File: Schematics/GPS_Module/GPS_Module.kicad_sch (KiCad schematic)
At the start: 0 parts

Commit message: added proccessor and added sam-m10q symbol
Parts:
- added C1: 10uf, Capacitor_THT:C_Radial_D5.0mm_H11.0mm_P2.00mm, symbol Device:C
- added C10, C9: 1uf, Capacitor_SMD:C_0402_1005Metric, symbol Device:C
- added C2, C4, C6, C7: 100nf, Capacitor_SMD:C_0402_1005Metric, symbol Device:C
- added C3, C5: 10pF, Capacitor_SMD:C_0402_1005Metric, symbol Device:C
- added C8: 10nf, Capacitor_SMD:C_0402_1005Metric, symbol Device:C
- added FB1: 120R, Inductor_SMD:L_0603_1608Metric, symbol Device:FerriteBead
- added U1: STM32F103CBTx, Package_QFP:LQFP-48_7x7mm_P0.5mm, symbol MCU_ST_STM32F1:STM32F103CBTx
- added U2: SAM-M10Q-00B, SAM-M10Q_UBL, symbol sam-m10q:SAM-M10Q-00B
- added Y1: 16MHz, Crystal:Crystal_SMD_2016-4Pin_2.0x1.6mm, symbol Device:Crystal_GND24
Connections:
- new net +3.3V: C1.1, C1.2, C10.1, C10.2, C2.1, C2.2, C3.2, C4.1, C4.2, C5.2, C6.1, C6.2, C7.1, C7.2, C8.2, C9.2, FB1.2, U1.1 (VBAT), U1.23 (VSS), U1.24 (VDD), U1.35 (VSS), U1.36 (VDD), U1.47 (VSS), U1.48 (VDD), U1.8 (VSSA), Y1.2, Y1.4
- new net +3.3VA: C8.1, C9.1, FB1.1, U1.9 (VDDA)
- new net OSC_IN: C3.1, U1.5 (PD0), Y1.1
- new net OSC_OUT: C5.1, U1.6 (PD1), Y1.3
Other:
- note added: "Additional Filtering to the Analogue VDD"
- note added: "CL = (CLcrystal - Cstray)* 2 YXC XL7EL89CKI-111YLC-16M Crystal"
- note added: "Crystal Oscillator"
- note added: "Decoupling Capacitors for VBAT and VDD"
- note added: "One 100nf "high quality ceramic" capacitor for each VDD and VBAT One 10uf electrolytic capacitor for bulk filtering. Place them as close as possible to the IC."

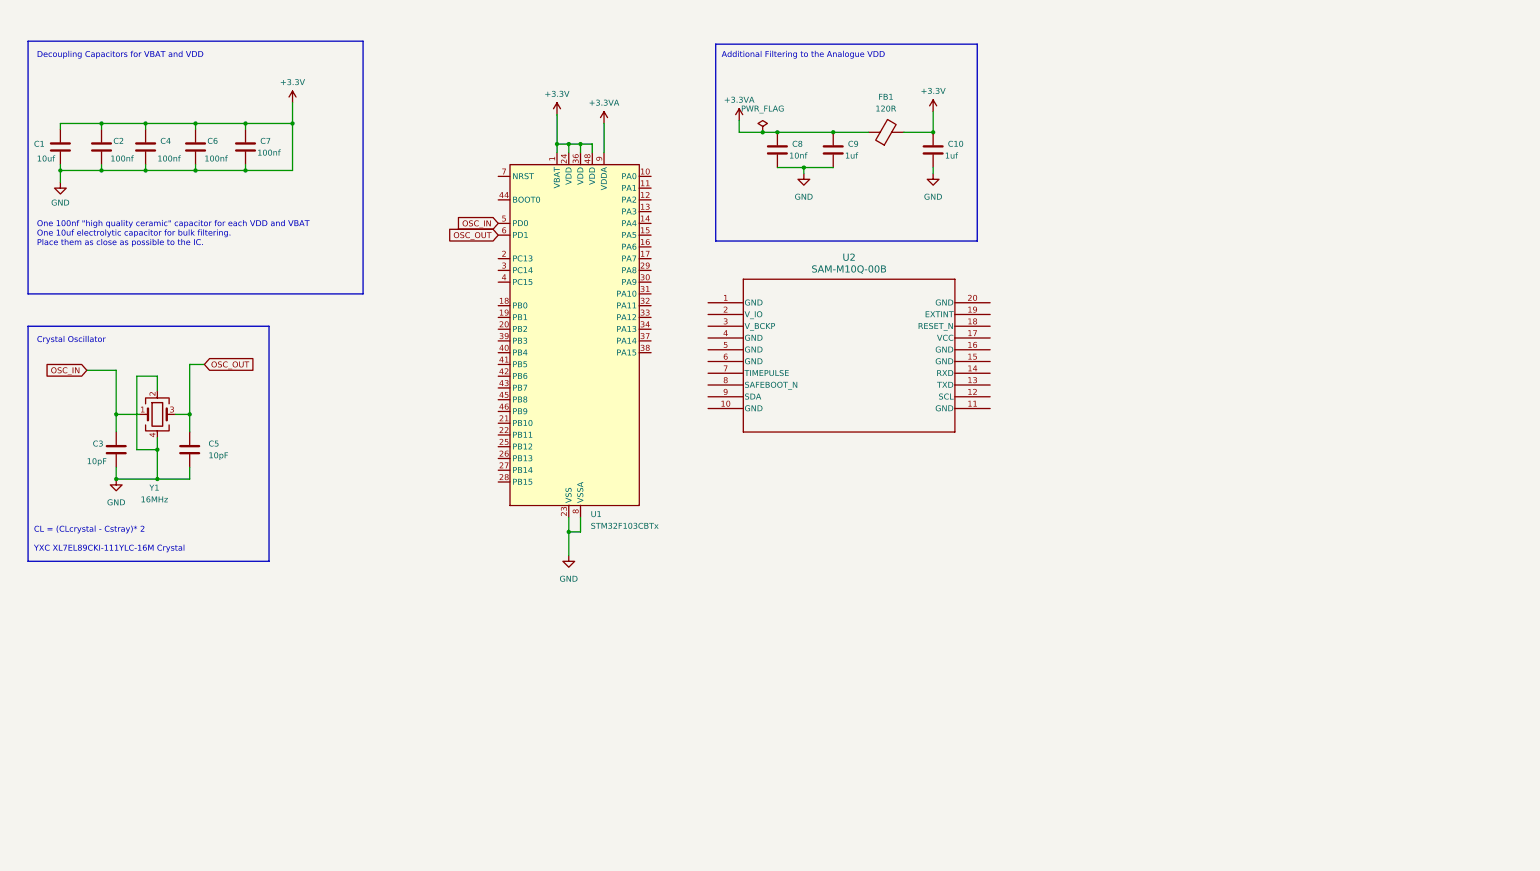
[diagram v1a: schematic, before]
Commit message: added GPS module from last year added labels to processor
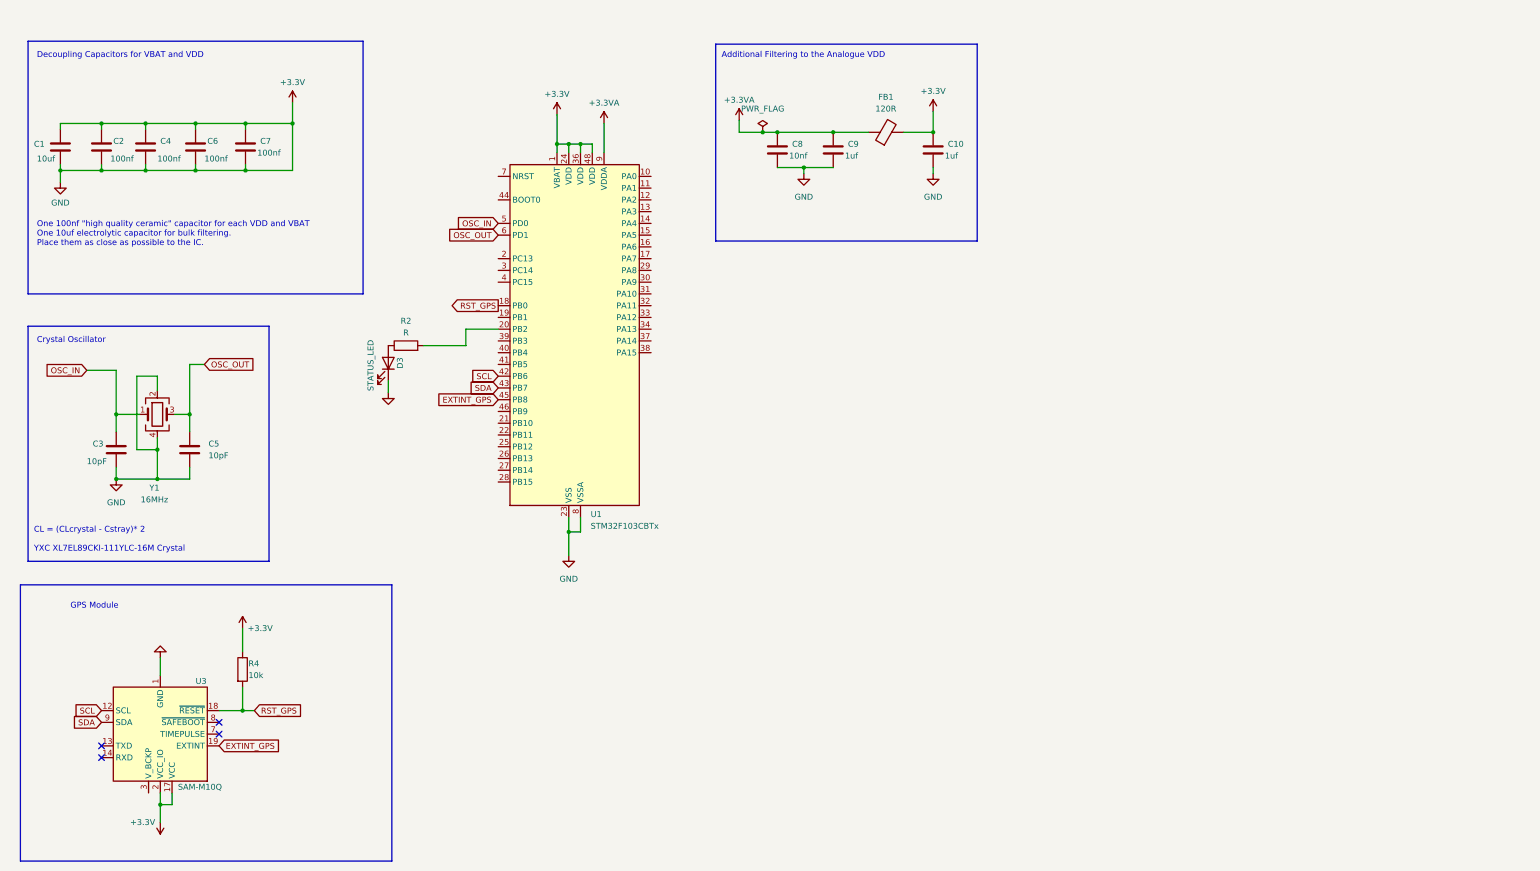
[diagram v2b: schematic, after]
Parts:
- removed U2: SAM-M10Q-00B, SAM-M10Q_UBL, symbol sam-m10q:SAM-M10Q-00B
- added D3: STATUS_LED, LED_SMD:LED_0805_2012Metric, symbol Device:LED
- added R2: R, symbol Device:R
- added R4: 10k, Resistor_SMD:R_0603_1608Metric, symbol Device:R
- added U3: SAM-M10Q, QRET_GPS_Footprints:U-blox_SAM-M8Q, symbol RF_GPS:SAM-M8Q
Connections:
- net +3.3V: now also D3.1 (K), R4.1, U3.1 (GND), U3.10 (GND), U3.11 (GND), U3.15 (GND), U3.16 (GND), U3.17 (VCC), U3.2 (VCC_IO), U3.20 (GND), U3.4 (GND), U3.5 (GND), U3.6 (GND)
- net RST_GPS: now reaches U1.18 (PB0)
- net RST_GPS: now also R4.2, U3.18 (~{RESET})
- net at U1.20 (PB2): now also R2.2
- net SCL: now reaches U1.42 (PB6)
- net SCL: now also U3.12 (SCL)
- net SDA: now reaches U1.43 (PB7)
- net SDA: now also U3.9 (SDA)
- net EXTINT_GPS: now reaches U1.45 (PB8)
- net EXTINT_GPS: now also U3.19 (EXTINT)
- new net: D3.2 (A), R2.1
- no-connect marks 0 -> 4
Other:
- note added: "GPS Module"

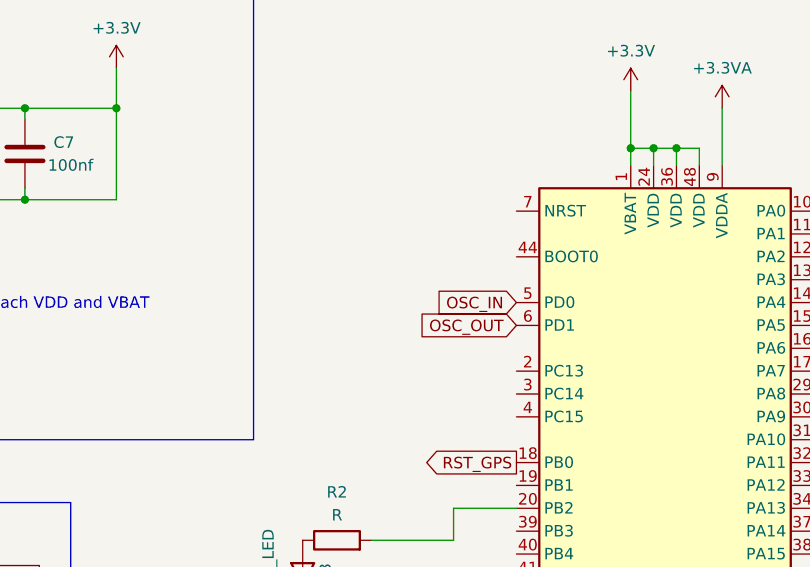
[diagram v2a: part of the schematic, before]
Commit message: Update GPS_Module.kicad_sch
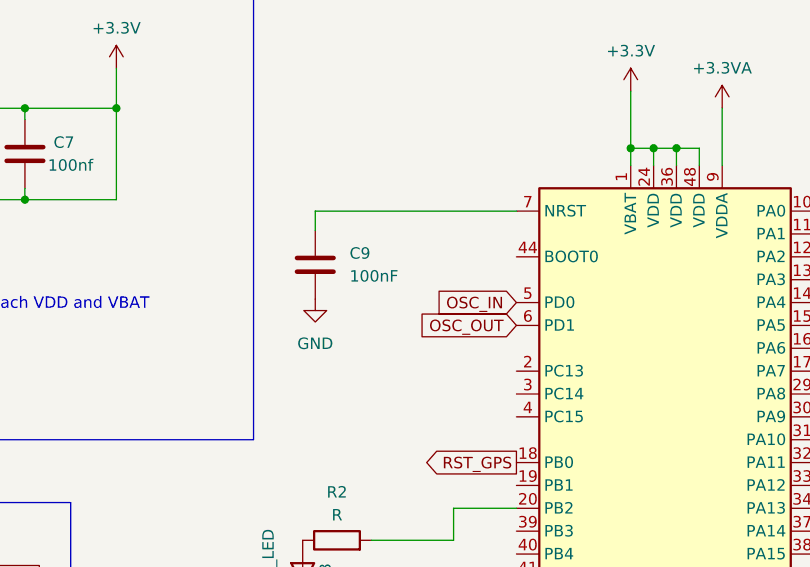
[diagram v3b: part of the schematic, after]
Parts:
- added C9: 100nF, Capacitor_SMD:C_0805_2012Metric, symbol Device:C
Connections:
- net +3.3V: now also C9.2
- net at U1.7 (NRST): now also C9.1
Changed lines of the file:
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@@
+    (stroke (width 0) (type default))
+  )
+  (wire (pts (xy 96.393 47.498) (xy 96.393 49.657))
     (stroke (width 0) (type default))
   )
@@
   )
   (wire (pts (xy 136.525 40.513) (xy 136.525 42.418))
+    (stroke (width 0) (type default))
+  )
+  (wire (pts (xy 118.745 47.498) (xy 96.393 47.498))
     (stroke (width 0) (type default))
   )
@@
         (path "/c9a01778-8bed-4fe7-bd5a-975b80c0ed6a"
           (reference "#PWR012") (unit 1)
+        )
+      )
+    )
+  )
+  (symbol (lib_id "Device:C") (at 96.393 53.467 0) (unit 1)
+    (in_bom yes) (on_board yes) (dnp no)
+    (property "Reference" "C9" (at 100.203 52.197 0)
+      (effects (font (size 1.27 1.27)) (justify left))
+    )
+    (property "Value" "100nF" (at 100.203 54.737 0)
+      (effects (font (size 1.27 1.27)) (justify left))
+    )
+    (property "Footprint" "Capacitor_SMD:C_0805_2012Metric" (at 97.3582 57.277 0)
+      (effects (font (size 1.27 1.27)) hide)
+    )
+    (property "Datasheet" "~" (at 96.393 53.467 0)
+      (effects (font (size 1.27 1.27)) hide)
+    )
+    (property "LCSC" "C49678" (at 96.393 53.467 0)
+      (effects (font (size 1.27 1.27)) hide)
+    )
+    (pin "1")
+    (pin "2")
+    (instances
+      (project "GPS_BOARD_COMPLETE_V1"
+        (path "/9b502ebe-f445-4c9b-a61b-230a013430f4"
+          (reference "C9") (unit 1)
+        )
+      )
+      (project "GPS_Module"
+        (path "/c9a01778-8bed-4fe7-bd5a-975b80c0ed6a"
+          (reference "C11") (unit 1)
         )
       )
@@
         )
       )
+    )
+  )
+  (symbol (lib_id "power:GND") (at 96.393 57.277 0) (unit 1)
+    (in_bom yes) (on_board yes) (dnp no) (fields_autoplaced)
+    (property "Reference" "#PWR015" (at 96.393 63.627 0)
+      (effects (font (size 1.27 1.27)) hide)
+    )
+    (property "Value" "GND" (at 96.393 62.23 0)
+      (effects (font (size 1.27 1.27)))
+    )
+    (property "Footprint" "" (at 96.393 57.277 0)
+      (effects (font (size 1.27 1.27)) hide)
+    )
+    (property "Datasheet" "" (at 96.393 57.277 0)
+      (effects (font (size 1.27 1.27)) hide)
+    )
+    (pin "1")
+    (instances
+      (project "GPS_Module"
+        (path "/c9a01778-8bed-4fe7-bd5a-975b80c0ed6a"
+          (reference "#PWR015") (unit 1)
+        )
+      )

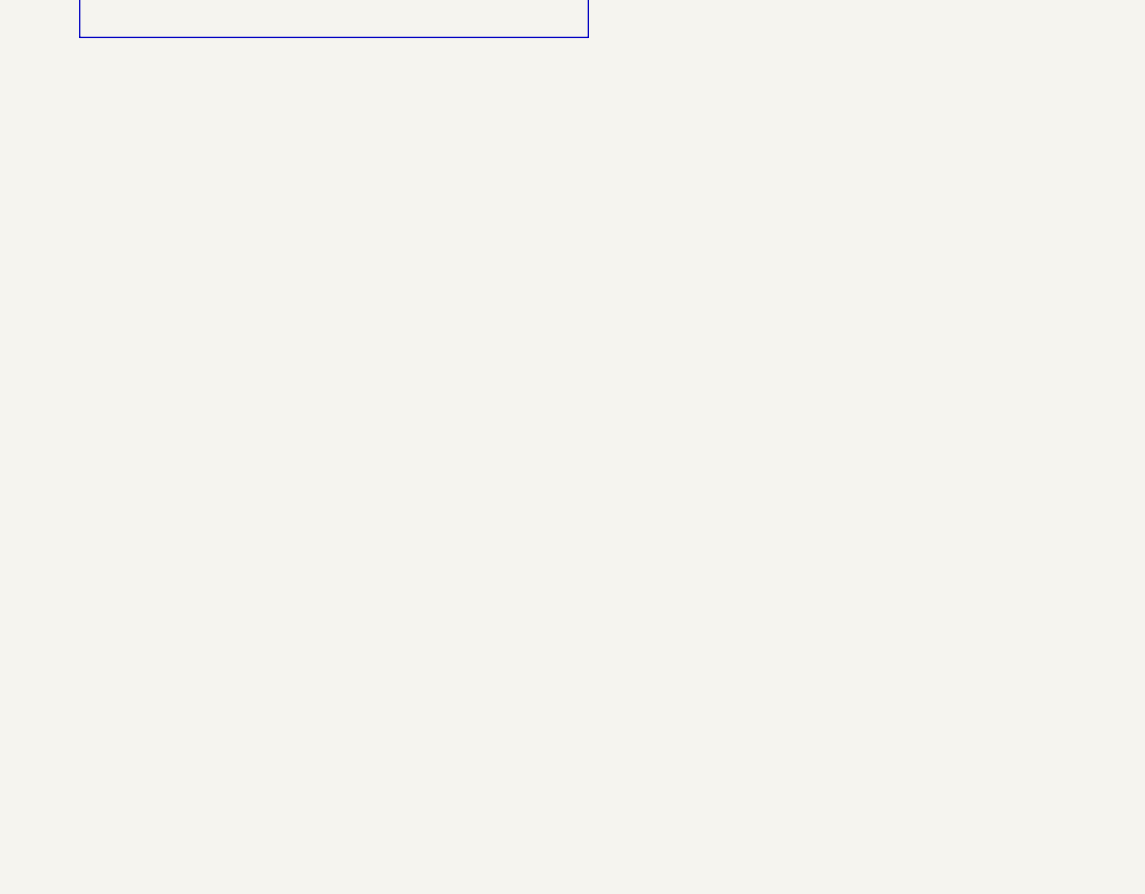
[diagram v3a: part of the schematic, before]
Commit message: Update GPS_Module.kicad_sch
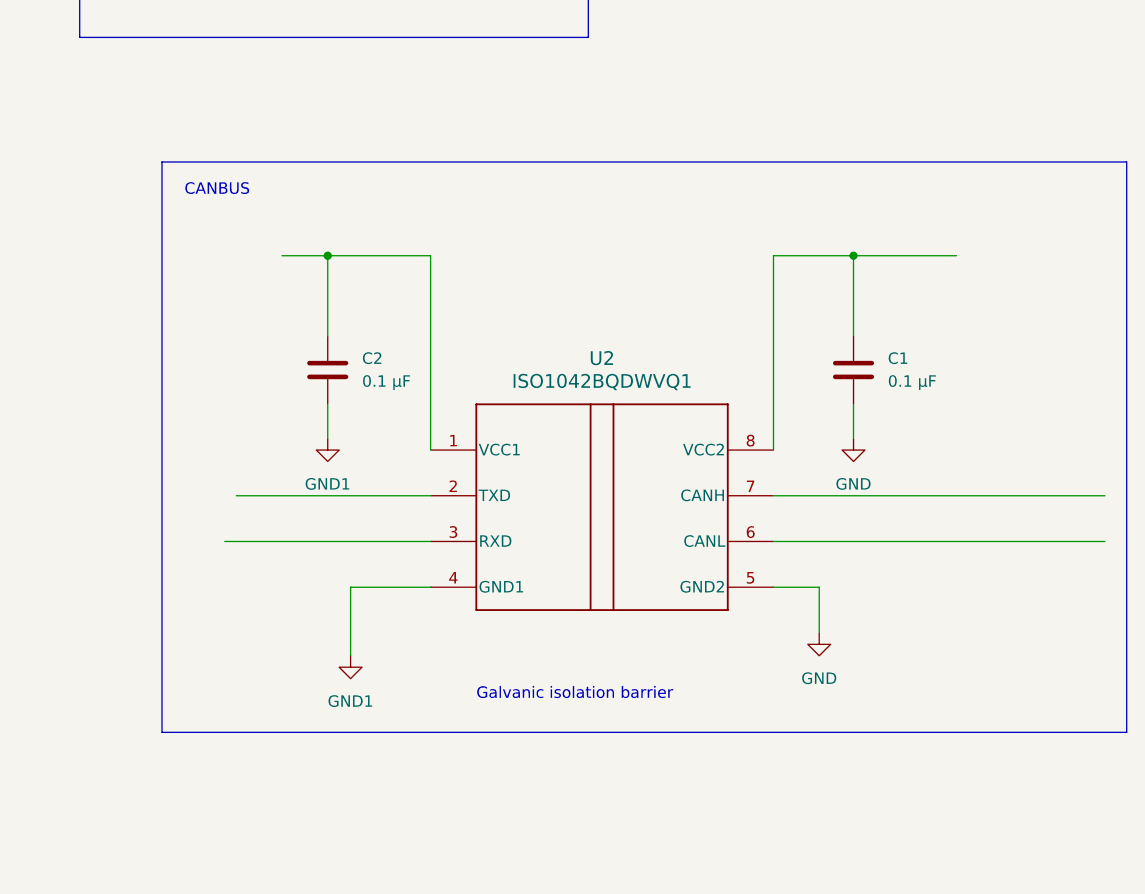
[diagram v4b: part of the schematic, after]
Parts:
- added C1, C2: 0.1 µF, symbol Device:C
- added U2: ISO1042BQDWVQ1, DWV0008A-IPC_A, symbol 2023-11-16_23-22-44:ISO1042BQDWVQ1
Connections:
- net +3.3V: now also C1.2, U2.5 (GND2)
- new net: C1.1, U2.8 (VCC2)
- new net: C2.1, U2.1 (VCC1)
- new net GND1: C2.2, U2.4 (GND1)
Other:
- note added: "CANBUS"
- note added: "Galvanic isolation barrier"

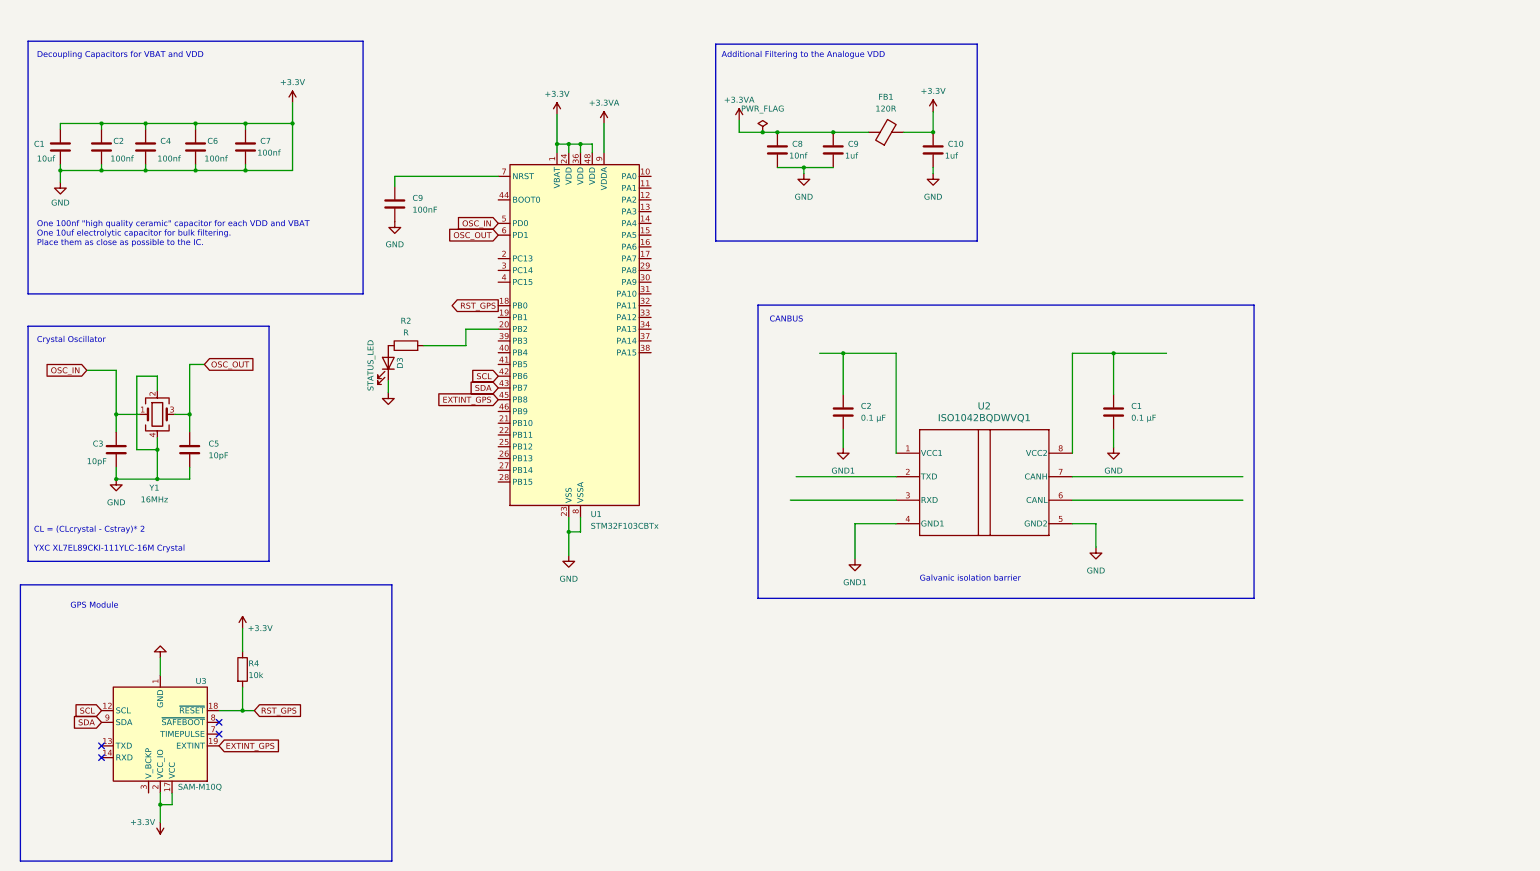
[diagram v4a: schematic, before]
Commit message: shrinked the CanBus subcircuit down
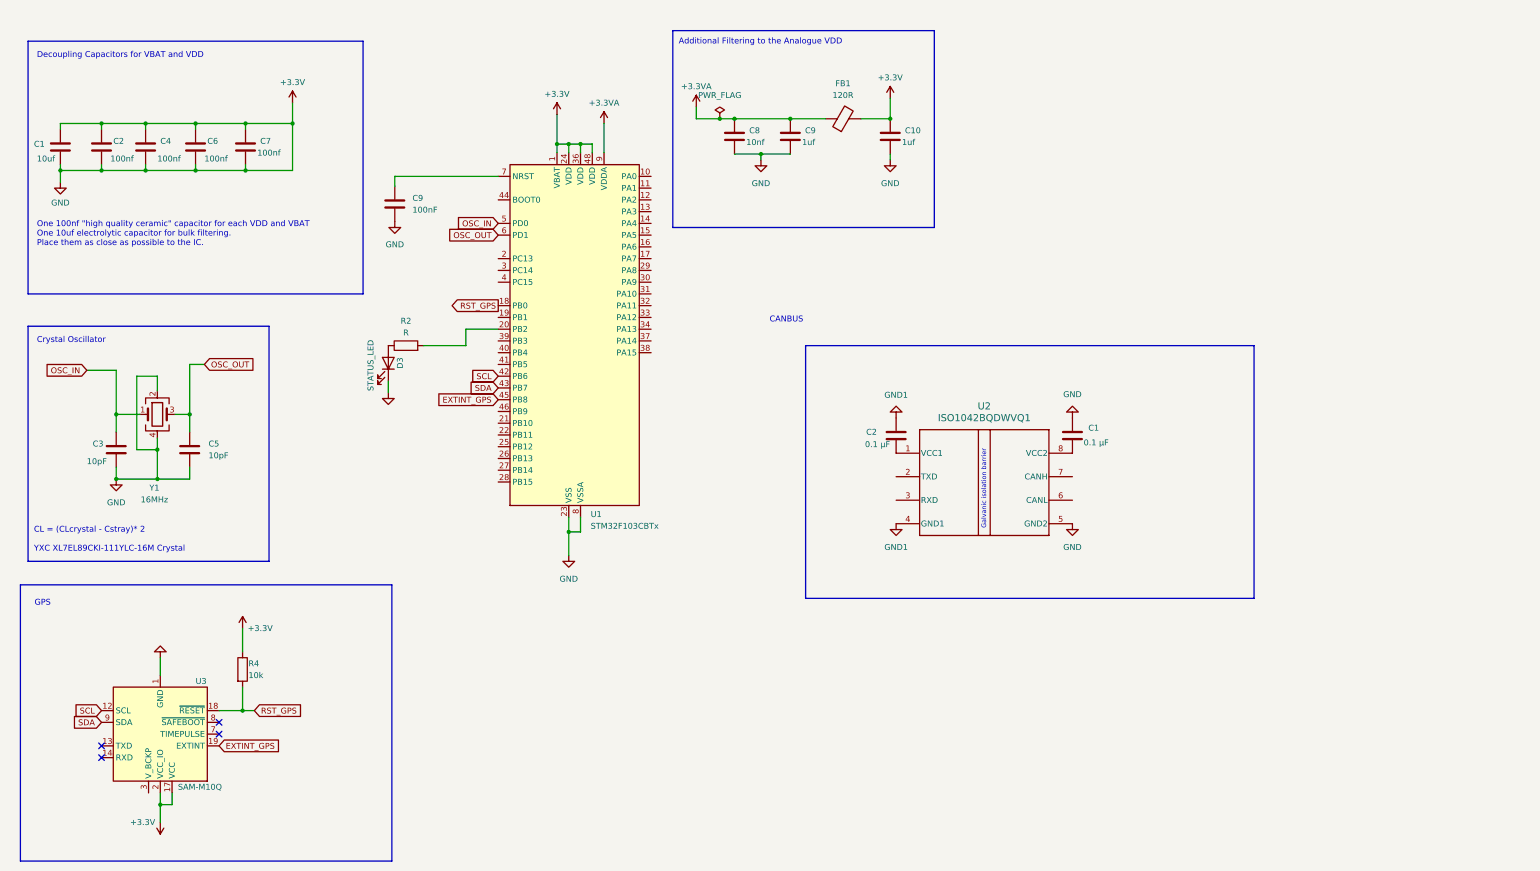
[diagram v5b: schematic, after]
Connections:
- net +3.3V: now also C1.1; no longer C1.2
- net GND1: now also C2.1; no longer C2.2
- net at U2.8 (VCC2): now also C1.2; no longer C1.1
- net at U2.1 (VCC1): now also C2.2; no longer C2.1
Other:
- note added: "GPS"
- note removed: "GPS Module"
- moved on the sheet: C10, C8, C9, FB1
